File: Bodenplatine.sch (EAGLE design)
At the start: 113 parts, among them K1 RY612012, K2 RY612012, K3 RY612012, K4 RY612012, K5 RY612012, K6 RY612012, K7 RY612012, K8 RY612012, K9 RY612012, Q1 BC846BLT1SMD, Q2 BC846BLT1SMD, Q3 BC846BLT1SMD, Q4 BC846BLT1SMD, Q5 BC846BLT1SMD, Q6 BC846BLT1SMD, Q7 BC846BLT1SMD, Q8 BC846BLT1SMD, Q9 BC846BLT1SMD, X1 SPRINGCON_AST125_5X2, X10 SPRINGCON_AST125_3X2, X11 SPRINGCON_AST125_4X2, X12 SPRINGCON_AST125_4X2, X13 SPRINGCON_AST125_5X2, X14 236-403, X15 236-402, X2 SPRINGCON_AST125_5X2, X3 SPRINGCON_AST125_5X2, X4 SPRINGCON_AST125_5X2, X5 SPRINGCON_AST125_5X2, X6 SPRINGCON_AST125_5X2, X7 SPRINGCON_AST125_5X2, X8 SPRINGCON_AST125_5X2, X9 SPRINGCON_AST125_5X2

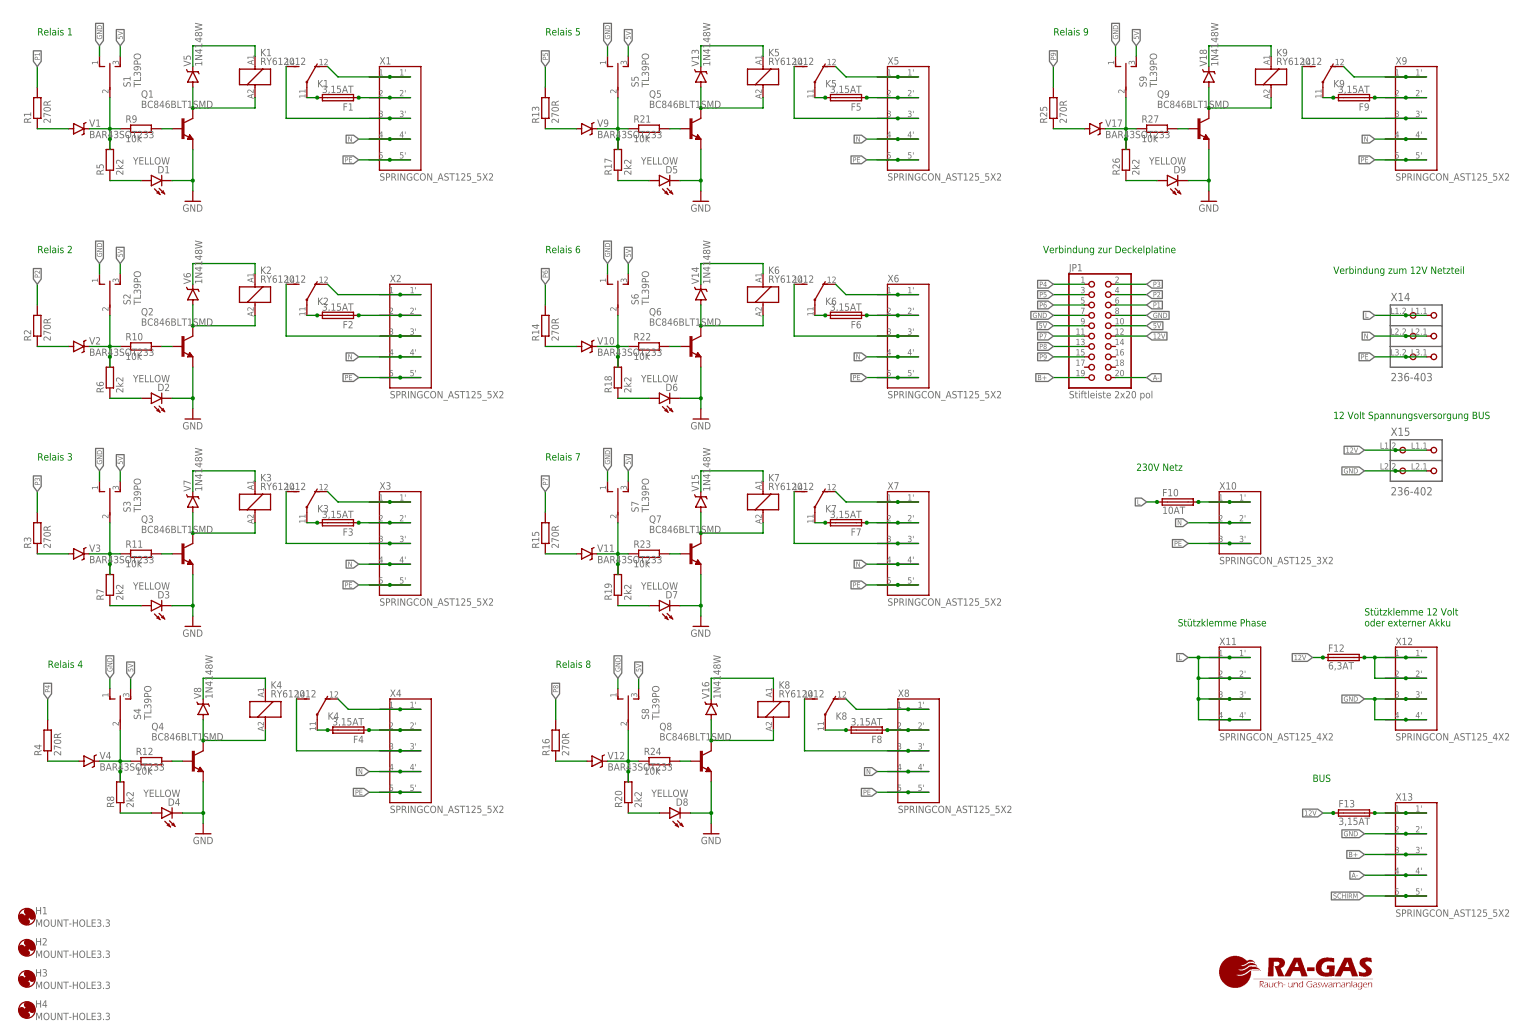
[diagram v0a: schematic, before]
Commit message: Import der Version v0.9.5
Aus dieser Version wurde der zweite Prototype erstellt. Der Produzent
war dieses Mal https://portal.multi-circuit-boards.eu
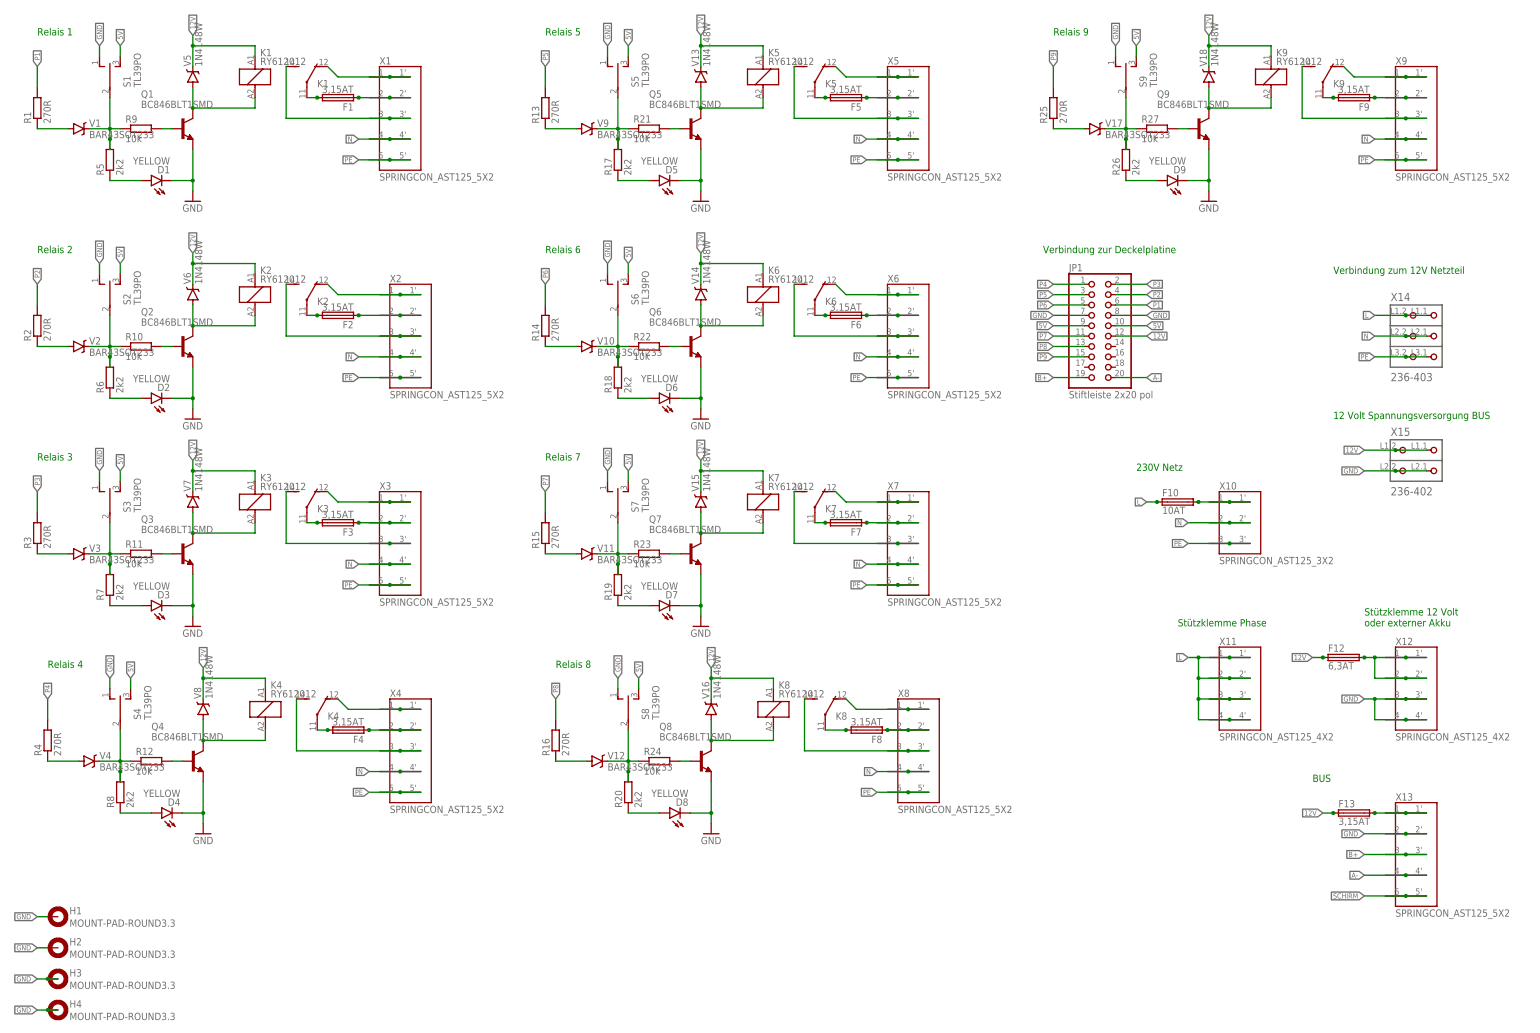
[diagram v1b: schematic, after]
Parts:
- H1, H2, H3, H4: value MOUNT-HOLE3.3 -> MOUNT-PAD-ROUND3.3; device holes:MOUNT-HOLE3.3 -> holes:MOUNT-PAD-ROUND3.3
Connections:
- removed net N$11: K21.1, V6.C
- removed net N$17: K31.1, V7.C
- removed net N$27: K41.1, V8.C
- removed net N$37: K51.1, V13.C
- removed net N$47: K61.1, V14.C
- removed net N$57: K71.1, V15.C
- removed net N$67: K81.1, V16.C
- removed net N$77: K91.1, V18.C
- removed net N$87: K11.1, V5.C
- net 12V: now also K11.1, K21.1, K31.1, K41.1, K51.1, K61.1, K71.1, K81.1, K91.1, V13.C, V14.C, V15.C, V16.C, V18.C, V5.C, V6.C, V7.C, V8.C
- net GND: now also H1.MOUNT, H2.MOUNT, H3.MOUNT, H4.MOUNT
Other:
- moved on the sheet: H1, H2, H3, H4

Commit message: Anschluss Deckelplatine gegen verdrehen gesichert
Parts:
- JP1: device pinhead:PINHD-2X10 -> xMZ-Mod-Touch-Bodenplatine:PINHD-2X10
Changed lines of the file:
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@@
 <attribute name="AUTHOR" value="Stefan Müller"/>
 <attribute name="PROJEKTNAME" value="xMZ-Mod-Touch-Bodenplatine"/>
-<attribute name="VERSION" value="0.9.5"/>
+<attribute name="VERSION" value="0.9.6"/>
 </attributes>
 <variantdefs>
@@
 <attribute name="OC_FARNELL" value="unknown"/>
 </part>
-<part name="JP1" library="pinhead" deviceset="PINHD-2X10" device="" value="Stiftleiste 2x20 pol">
+<part name="JP1" library="xMZ-Mod-Touch-Bodenplatine" deviceset="PINHD-2X10" device="" value="Stiftleiste 2x20 pol">
 <attribute name="MF" value="TE CONNECTIVITY / AMP"/>
 <attribute name="MPN" value="825440-5"/>
